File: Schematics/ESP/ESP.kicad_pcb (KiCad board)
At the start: 2 copper layers, 180.5 x 111.7 mm, 87 parts, among them J1 Barrel_Jack, J11 Bumper 1, J12 Bumper 2, J13 Battery Input, J14 Conn_02x19_Odd_Even, J15 UltraSconic B, J16 Conn_02x19_Odd_Even, J2 IMU, J3 Battery charger, J4 Motor A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

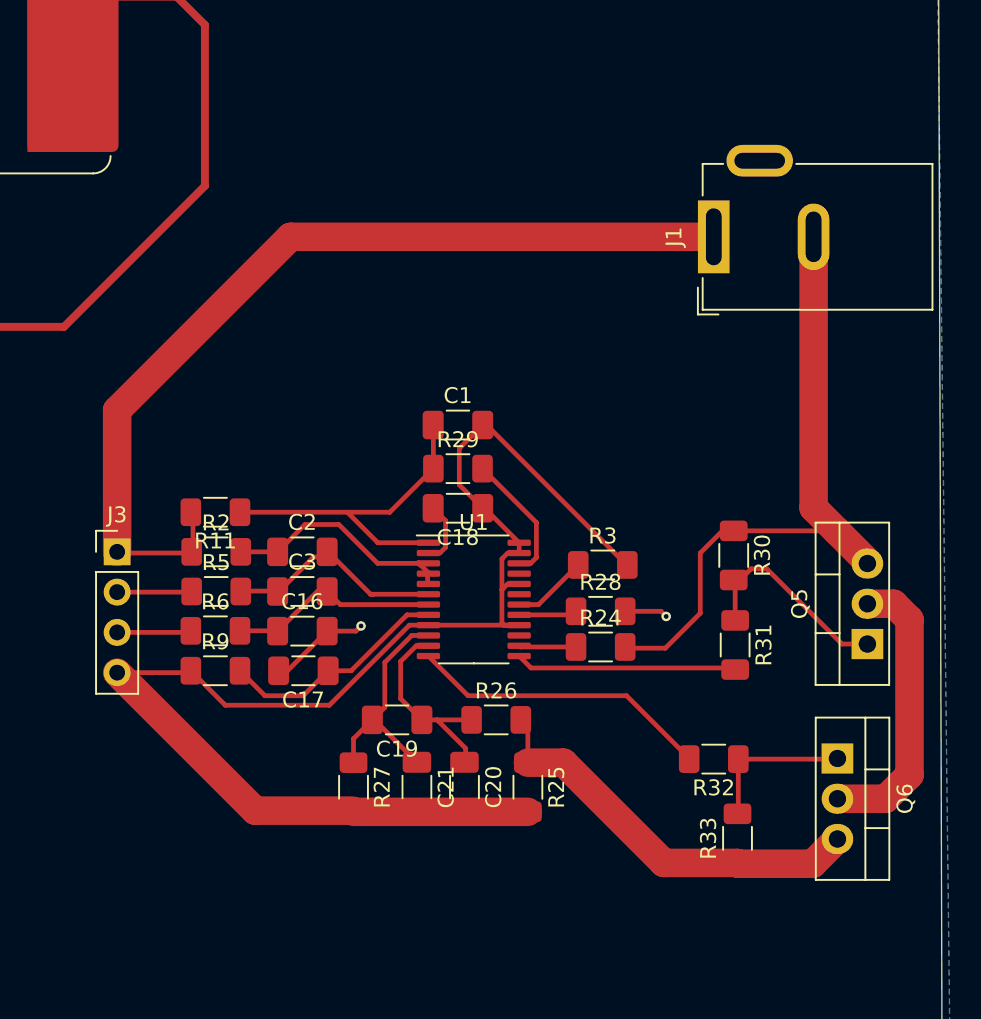
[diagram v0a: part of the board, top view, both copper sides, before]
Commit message: charging IC PCB spacing cleanup
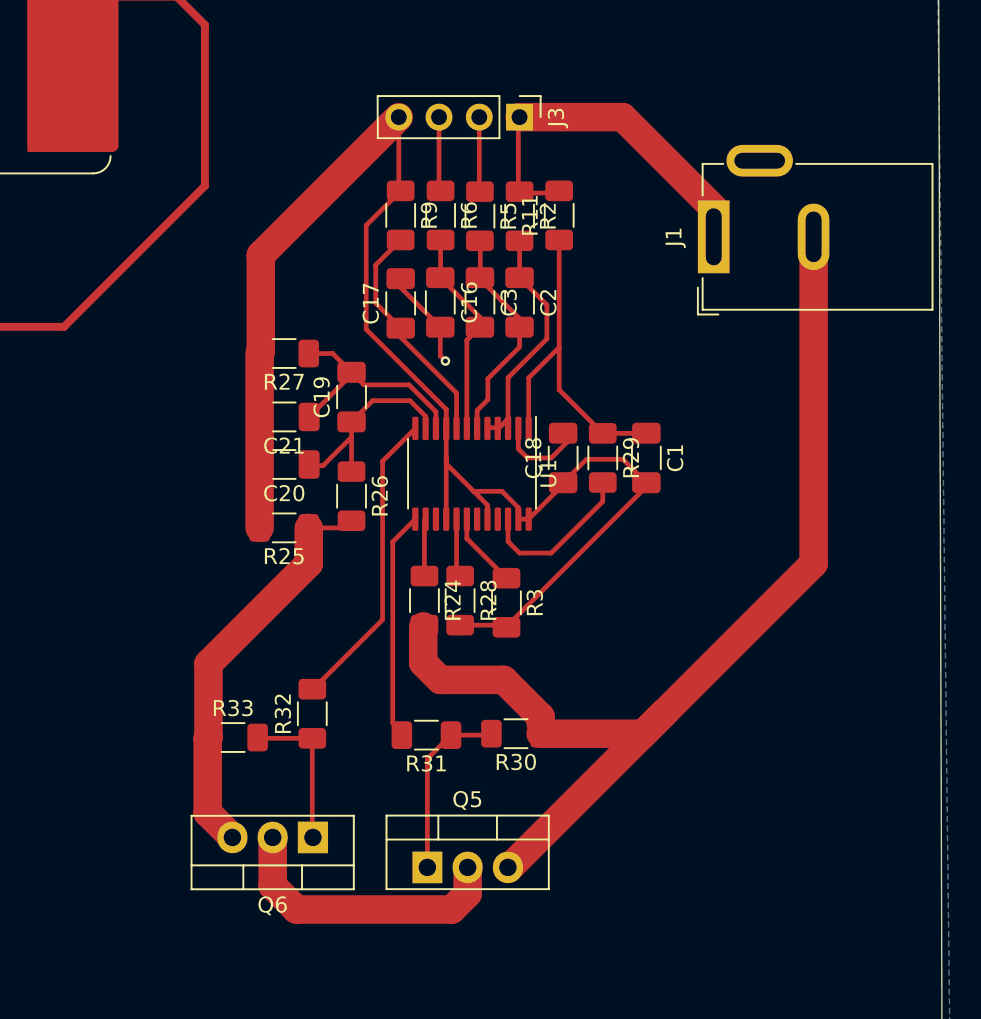
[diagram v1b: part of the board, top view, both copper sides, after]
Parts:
- moved J3 37.4 mm to (204.0, 112.5), turned to -90 degrees
- moved Q6 33.5 mm to (191.0, 157.9), turned to 180 degrees
- moved R33 32.5 mm to (185.9, 151.6), turned to 0 degrees
- moved Q5 31.1 mm to (198.2, 159.8), turned to 0 degrees
- moved R9 31.0 mm to (196.5, 118.7), turned to -90 degrees
- moved R6 29.8 mm to (199.0, 118.7), turned to -90 degrees
- moved R5 28.9 mm to (201.5, 118.8), turned to -90 degrees
- moved R11 28.7 mm to (206.5, 118.7), turned to 90 degrees
- moved R2 28.5 mm to (204.0, 118.8), turned to -90 degrees
- moved R27 27.7 mm to (189.2, 127.4), turned to 180 degrees
- moved R32 25.5 mm to (190.9, 150.1), turned to 90 degrees
- moved C21 24.8 mm to (189.2, 131.4), turned to 180 degrees
- moved C17 24.0 mm to (196.5, 124.2), turned to 90 degrees
- moved C20 23.3 mm to (189.2, 134.4), turned to 180 degrees
- moved C16 22.5 mm to (199.0, 124.2), turned to -90 degrees
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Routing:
- net Cell3+: track 57.5 -> 22.8 mm
- net P-: track 39.7 -> 67.5 mm
- net Net-(U1-PRES): track 8.26 -> 10.2 mm
- net Net-(Q5-G): track 13.0 -> 11.2 mm
- net Net-(U1-AVDD): track 4.03 -> 5.68 mm
- net Battery-: track 166.4 -> 167.8 mm, vias 23 -> 22
- net CHG: track 13.8 -> 14.4 mm

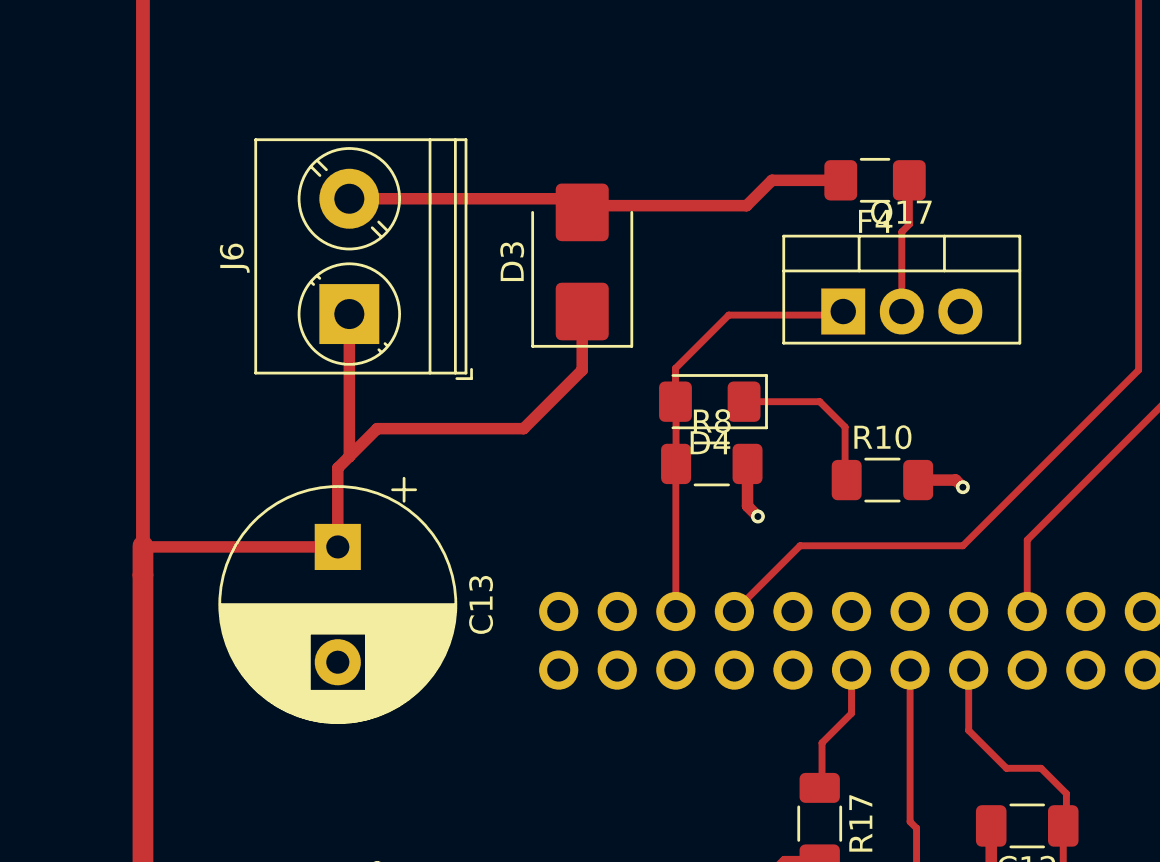
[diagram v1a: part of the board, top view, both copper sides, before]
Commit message: removed fan related stuff
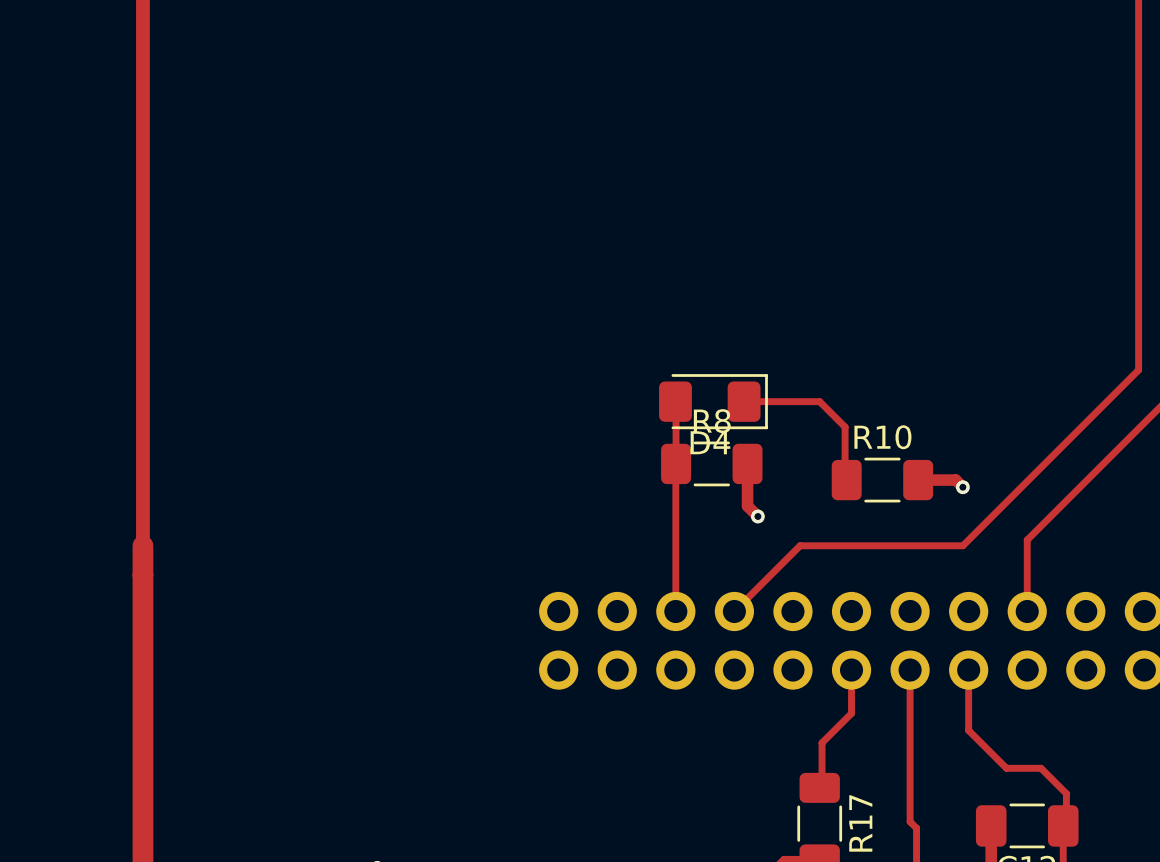
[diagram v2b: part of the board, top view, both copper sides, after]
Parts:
- removed C13: 680u, Capacitor_THT:CP_Radial_D10.0mm_P5.00mm
- removed D3: PMEG045V050EPDZ, Diode_SMD:D_SMB
- removed F4: 0.72A, Fuse:Fuse_1206_3216Metric_Pad1.42x1.75mm_HandSolder
- removed J6: Fan, TerminalBlock_Phoenix:TerminalBlock_Phoenix_PT-1,5-2-5.0-H_1x02_P5.00mm_Horizontal
- removed Q17: PJP18N20, Package_TO_SOT_THT:TO-220-3_Vertical
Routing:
- net +12V: track 269.2 -> 236.3 mm
- net Net-(D3-A): track 21.5 -> 0.00 mm
- net Fan Signal: track 18.7 -> 9.06 mm
- net Net-(Q17-D): track 5.99 -> 0.00 mm

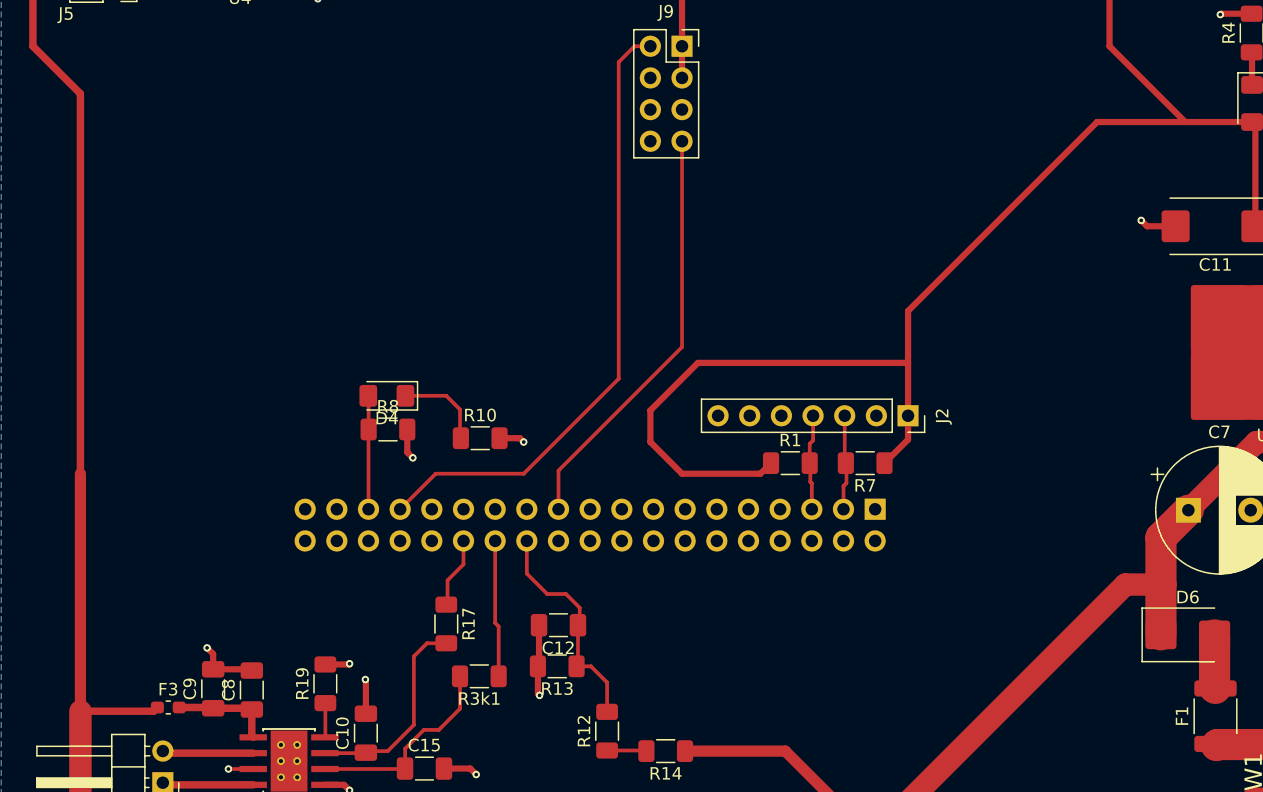
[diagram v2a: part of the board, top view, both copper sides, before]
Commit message: fixed 3.3v for IMU
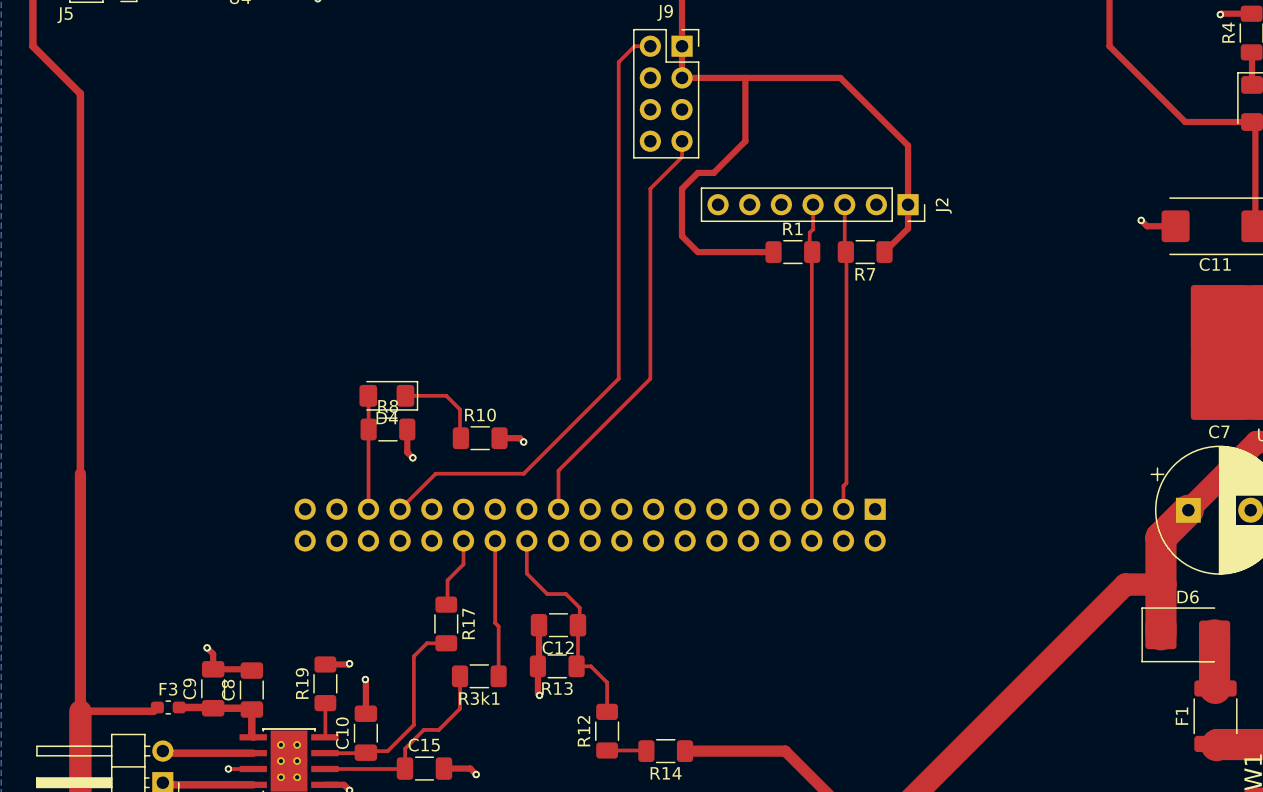
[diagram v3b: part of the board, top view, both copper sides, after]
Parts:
- R25: value 1m -> 10m
- moved R1 16.9 mm to (114.3, 115.6)
- moved R7 16.9 mm to (120.1, 115.6)
- moved J2 16.9 mm to (123.5, 111.8)
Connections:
- J2 pad 1: +5V -> +3.3V
- R1 pad 1: +5V -> +3.3V
- R7 pad 1: +5V -> +3.3V
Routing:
- net +5V: track 261.0 -> 183.7 mm
- net +3.3V: track 24.8 -> 77.9 mm
- net Net-(J16-Pin_5): track 7.61 -> 24.6 mm
- net Net-(J16-Pin_3): track 7.46 -> 24.4 mm
